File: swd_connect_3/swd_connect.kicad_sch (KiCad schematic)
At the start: 2 parts, among them J1 Link-E Receptacle, J2 swd-connect-3

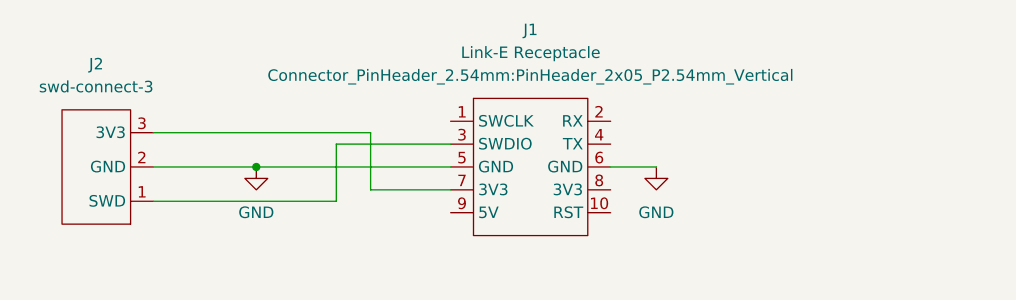
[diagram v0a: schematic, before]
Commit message: Update footprints to include silkscreen pin identifiers
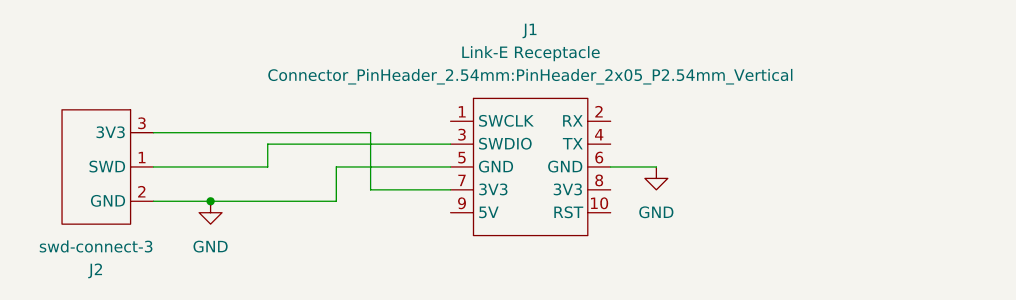
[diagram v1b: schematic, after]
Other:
- moved on the sheet: J2
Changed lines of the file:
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@@
     (comment 1 "(c) 2023")
   )
-  (junction (at 140.97 92.71) (diameter 0) (color 0 0 0 0)
+  (junction (at 135.89 96.52) (diameter 0) (color 0 0 0 0)
   )
   (wire (pts (xy 153.67 95.25) (xy 162.56 95.25))
     (stroke (width 0) (type default))
   )
-  (wire (pts (xy 129.54 92.71) (xy 140.97 92.71))
-    (stroke (width 0) (type default))
-  )
-  (wire (pts (xy 149.86 96.52) (xy 149.86 90.17))
+  (wire (pts (xy 149.86 92.71) (xy 162.56 92.71))
     (stroke (width 0) (type default))
   )
@@
     (stroke (width 0) (type default))
   )
-  (wire (pts (xy 149.86 90.17) (xy 162.56 90.17))
+  (wire (pts (xy 142.24 92.71) (xy 142.24 90.17))
+    (stroke (width 0) (type default))
+  )
+  (wire (pts (xy 129.54 92.71) (xy 142.24 92.71))
     (stroke (width 0) (type default))
   )
@@
     (stroke (width 0) (type default))
   )
-  (wire (pts (xy 129.54 96.52) (xy 149.86 96.52))
+  (wire (pts (xy 149.86 96.52) (xy 149.86 92.71))
     (stroke (width 0) (type default))
   )
-  (wire (pts (xy 140.97 92.71) (xy 162.56 92.71))
+  (wire (pts (xy 129.54 96.52) (xy 135.89 96.52))
+    (stroke (width 0) (type default))
+  )
+  (wire (pts (xy 142.24 90.17) (xy 162.56 90.17))
+    (stroke (width 0) (type default))
+  )
+  (wire (pts (xy 135.89 96.52) (xy 149.86 96.52))
     (stroke (width 0) (type default))
   )
@@
     )
   )
-  (symbol (lib_id "power:GND") (at 140.97 92.71 0) (unit 1)
+  (symbol (lib_id "power:GND") (at 135.89 96.52 0) (unit 1)
     (in_bom yes) (on_board yes) (dnp no) (fields_autoplaced)
-    (property "Reference" "#PWR01" (at 140.97 99.06 0)
+    (property "Reference" "#PWR01" (at 135.89 102.87 0)
       (effects (font (size 1.27 1.27)) hide)
     )
-    (property "Value" "GND" (at 140.97 97.79 0)
+    (property "Value" "GND" (at 135.89 101.6 0)
       (effects (font (size 1.27 1.27)))
     )
-    (property "Footprint" "" (at 140.97 92.71 0)
+    (property "Footprint" "" (at 135.89 96.52 0)
       (effects (font (size 1.27 1.27)) hide)
     )
-    (property "Datasheet" "" (at 140.97 92.71 0)
+    (property "Datasheet" "" (at 135.89 96.52 0)
       (effects (font (size 1.27 1.27)) hide)
     )
@@
     )
   )
-  (symbol (lib_id "swd-connect:swd-connect-3") (at 123.19 92.71 180) (unit 1)
-    (in_bom no) (on_board yes) (dnp no) (fields_autoplaced)
-    (property "Reference" "J2" (at 123.19 81.28 0)
+  (symbol (lib_id "swd-connect:swd-connect-3") (at 123.19 92.71 0) (mirror y) (unit 1)
+    (in_bom no) (on_board yes) (dnp no)
+    (property "Reference" "J2" (at 123.19 104.14 0)
       (effects (font (size 1.27 1.27)))
     )
-    (property "Value" "swd-connect-3" (at 123.19 83.82 0)
+    (property "Value" "swd-connect-3" (at 123.19 101.6 0)
       (effects (font (size 1.27 1.27)))
     )
-    (property "Footprint" "swd-connect:swd-connect-3-programmer" (at 123.19 85.09 0)
+    (property "Footprint" "swd-connect:swd-connect-3-programmer" (at 123.19 100.33 0)
       (effects (font (size 1.27 1.27)) hide)
     )
-    (property "Datasheet" "" (at 124.46 95.25 0)
+    (property "Datasheet" "" (at 124.46 90.17 0)
       (effects (font (size 1.27 1.27)) hide)
     )

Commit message: Update symbol to reflect the actual layout
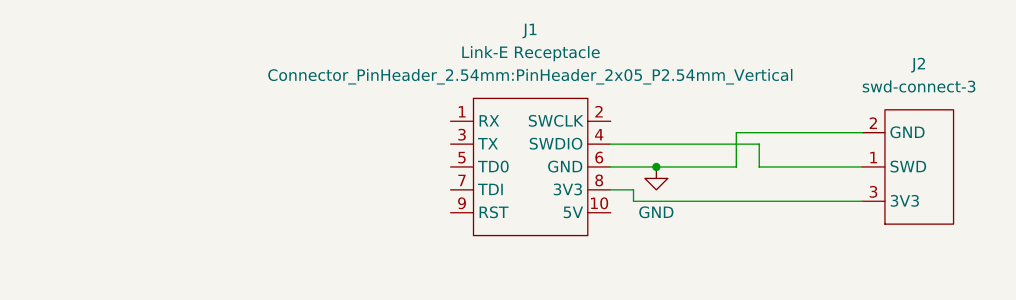
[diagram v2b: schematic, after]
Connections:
- net GND: no longer J1.5 (GND)
- net at J1.3 (TX): no longer J2.1 (SWD)
- net at J1.4 (SWDIO): now also J2.1 (SWD)
- net at J1.7 (TDI): no longer J2.3 (3V3)
- net at J1.8 (3V3): now also J2.3 (3V3)
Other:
- moved on the sheet: J2
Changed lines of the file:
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@@
     (comment 1 "(c) 2023")
   )
-  (junction (at 135.89 96.52) (diameter 0) (color 0 0 0 0)
+  (junction (at 185.42 92.71) (diameter 0) (color 0 0 0 0)
   )
-  (wire (pts (xy 153.67 95.25) (xy 162.56 95.25))
+  (wire (pts (xy 208.28 88.9) (xy 194.31 88.9))
     (stroke (width 0) (type default))
   )
-  (wire (pts (xy 149.86 92.71) (xy 162.56 92.71))
+  (wire (pts (xy 196.85 90.17) (xy 180.34 90.17))
     (stroke (width 0) (type default))
   )
-  (wire (pts (xy 129.54 88.9) (xy 153.67 88.9))
+  (wire (pts (xy 208.28 96.52) (xy 182.88 96.52))
     (stroke (width 0) (type default))
   )
-  (wire (pts (xy 142.24 92.71) (xy 142.24 90.17))
+  (wire (pts (xy 194.31 92.71) (xy 185.42 92.71))
     (stroke (width 0) (type default))
   )
-  (wire (pts (xy 129.54 92.71) (xy 142.24 92.71))
+  (wire (pts (xy 196.85 92.71) (xy 196.85 90.17))
     (stroke (width 0) (type default))
   )
-  (wire (pts (xy 153.67 88.9) (xy 153.67 95.25))
+  (wire (pts (xy 194.31 88.9) (xy 194.31 92.71))
     (stroke (width 0) (type default))
   )
-  (wire (pts (xy 149.86 96.52) (xy 149.86 92.71))
+  (wire (pts (xy 182.88 96.52) (xy 182.88 95.25))
     (stroke (width 0) (type default))
   )
-  (wire (pts (xy 129.54 96.52) (xy 135.89 96.52))
-    (stroke (width 0) (type default))
-  )
-  (wire (pts (xy 142.24 90.17) (xy 162.56 90.17))
-    (stroke (width 0) (type default))
-  )
-  (wire (pts (xy 135.89 96.52) (xy 149.86 96.52))
+  (wire (pts (xy 182.88 95.25) (xy 180.34 95.25))
     (stroke (width 0) (type default))
   )
   (wire (pts (xy 180.34 92.71) (xy 185.42 92.71))
+    (stroke (width 0) (type default))
+  )
+  (wire (pts (xy 208.28 92.71) (xy 196.85 92.71))
     (stroke (width 0) (type default))
   )
@@
     )
   )
-  (symbol (lib_id "power:GND") (at 135.89 96.52 0) (unit 1)
-    (in_bom yes) (on_board yes) (dnp no) (fields_autoplaced)
-    (property "Reference" "#PWR01" (at 135.89 102.87 0)
-      (effects (font (size 1.27 1.27)) hide)
-    )
-    (property "Value" "GND" (at 135.89 101.6 0)
-      (effects (font (size 1.27 1.27)))
-    )
-    (property "Footprint" "" (at 135.89 96.52 0)
-      (effects (font (size 1.27 1.27)) hide)
-    )
-    (property "Datasheet" "" (at 135.89 96.52 0)
-      (effects (font (size 1.27 1.27)) hide)
-    )
-    (pin "1")
-    (instances
-      (project "swd_connect"
-        (path "/318193d7-876b-4e23-b273-ef52b6ed065b"
-          (reference "#PWR01") (unit 1)
-        )
-      )
-    )
-  )
   (symbol (lib_id "power:GND") (at 185.42 92.71 0) (unit 1)
     (in_bom yes) (on_board yes) (dnp no) (fields_autoplaced)
@@
     )
   )
-  (symbol (lib_id "swd-connect:swd-connect-3") (at 123.19 92.71 0) (mirror y) (unit 1)
+  (symbol (lib_id "swd-connect:swd-connect-3") (at 214.63 92.71 0) (mirror x) (unit 1)
     (in_bom no) (on_board yes) (dnp no)
-    (property "Reference" "J2" (at 123.19 104.14 0)
+    (property "Reference" "J2" (at 214.63 81.28 0)
       (effects (font (size 1.27 1.27)))
     )
-    (property "Value" "swd-connect-3" (at 123.19 101.6 0)
+    (property "Value" "swd-connect-3" (at 214.63 83.82 0)
       (effects (font (size 1.27 1.27)))
     )
-    (property "Footprint" "swd-connect:swd-connect-3-programmer" (at 123.19 100.33 0)
+    (property "Footprint" "swd-connect:swd-connect-3-programmer" (at 214.63 85.09 0)
       (effects (font (size 1.27 1.27)) hide)
     )
-    (property "Datasheet" "" (at 124.46 90.17 0)
+    (property "Datasheet" "" (at 213.36 95.25 0)
       (effects (font (size 1.27 1.27)) hide)
     )

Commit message: Updated swd connect
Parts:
- J2: footprint swd-connect:swd-connect-3-programmer -> swd-connect:swd-connect-3-programmer-tight
